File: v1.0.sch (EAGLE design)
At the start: 169 parts, among them J1 DC-044-A, J2 MICROSD-9P, J3 2p-2.54, J4 2p-2.54, Q1 SI4532ADY, Q3 6pF@32.7680kHz, SW1 SW-200D, SW2 SW-200D, U1 MCP23017-E/SO, U10 74HC139N, U11 BZX84C30, U2 MCP79412-I/SN, U3 LOPY, U4 GROVE_DC&DC, U5 LM1085IT-5.0, U6 FT232RL-SSOP28, U7 2x14p-2.54, U8 FT232RL-SSOP28, U9 SP483ECN-L, X1 JST-XH-05-PIN-ROUND-PAD, X10 JST-XH-07-PIN-ROUND-PAD, X11 JST-XH-07-PIN-ROUND-PAD, X12 JST-XH-07-PIN-ROUND-PAD, X13 JST-XH-05-PIN-ROUND-PAD, X14 JST-XH-05-PIN-ROUND-PAD, X15 JST-XH-05-PIN-ROUND-PAD, X16 JST-XH-05-PIN-ROUND-PAD, X17 JST-XH-05-PIN-ROUND-PAD, X18 JST-XH-05-PIN-ROUND-PAD, X19 JST-XH-05-PIN-ROUND-PAD, X2 JST-XH-05-PIN-ROUND-PAD, X20 JST-XH-05-PIN-ROUND-PAD, X21 JST-XH-05-PIN-ROUND-PAD, X22 JST-XH-07-PIN-ROUND-PAD, X23 JST-XH-05-PIN-ROUND-PAD, X24 JST-XH-07-PIN-ROUND-PAD, X25 JST-XH-07-PIN-ROUND-PAD, X27 JST-XH-07-PIN-ROUND-PAD, X28 JST-XH-05-PIN-ROUND-PAD, X3 JST-XH-05-PIN-ROUND-PAD, X4 JST-XH-07-PIN-ROUND-PAD, X5 JST-XH-07-PIN-ROUND-PAD, X6 JST-XH-07-PIN-ROUND-PAD, X7 JST-XH-07-PIN-ROUND-PAD, X8 JST-XH-07-PIN-ROUND-PAD, X9 JST-XH-07-PIN-ROUND-PAD

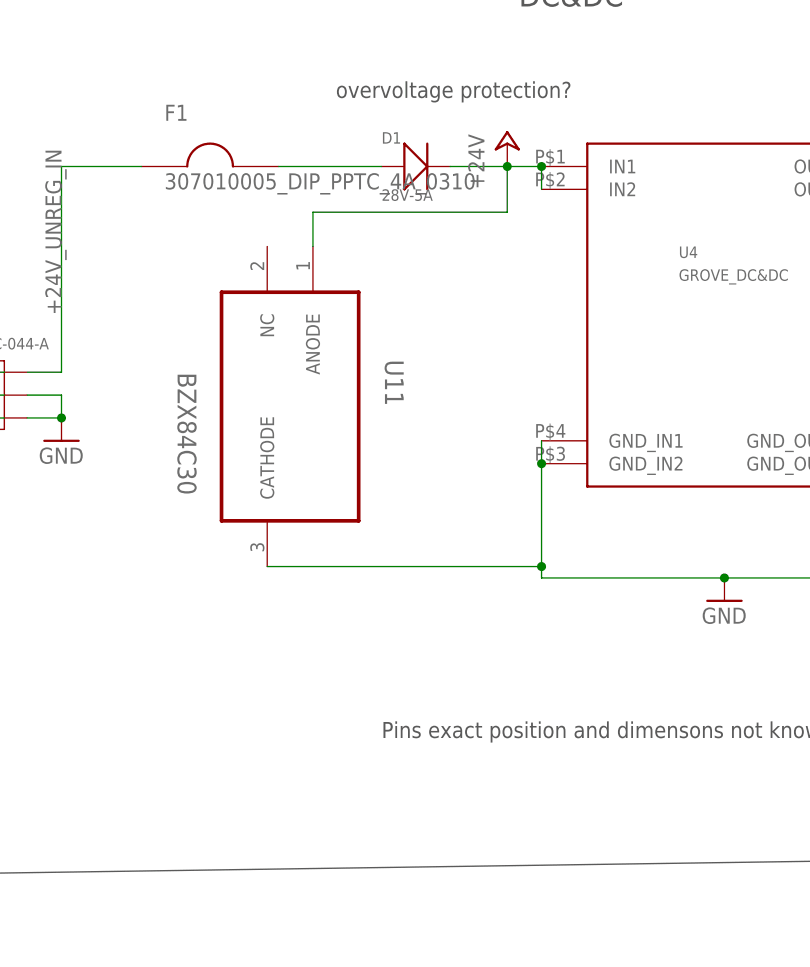
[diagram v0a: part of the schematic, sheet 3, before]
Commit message: overvoltage
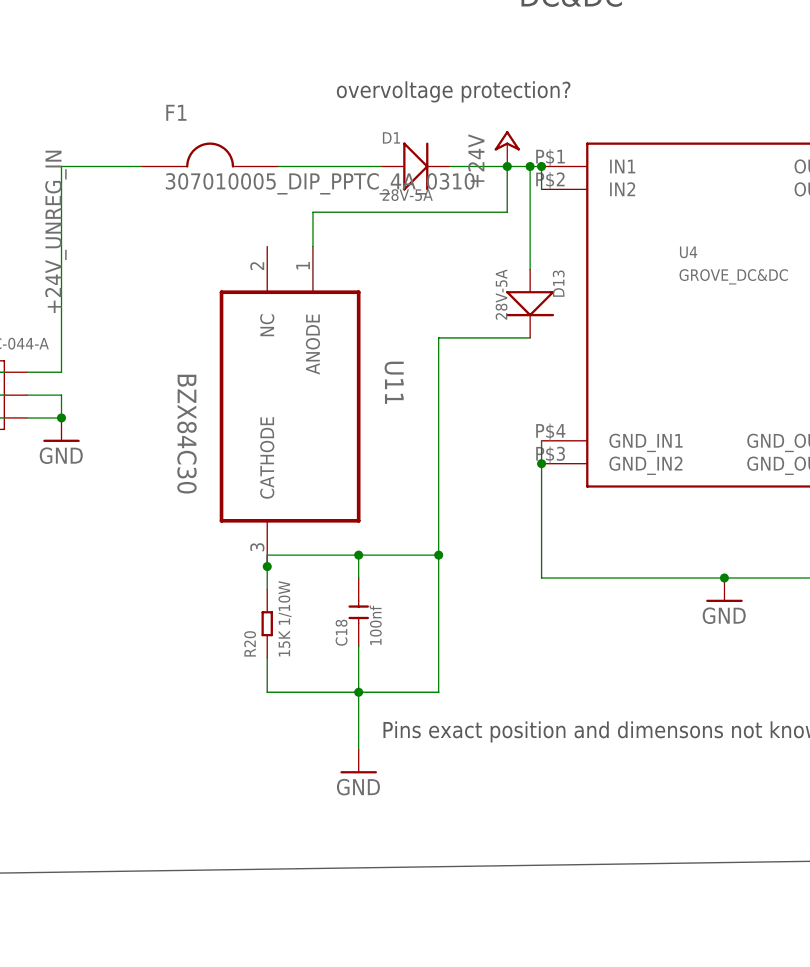
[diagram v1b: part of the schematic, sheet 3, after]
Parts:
- added C18: 100nf, Seeed-Capacitor:CERAMIC-100NF-50V-10%-X7R(0603)
- added D13: 28V-5A, Seeed-Diode-2016:SMD-DIODE-SCHOTTKY-28V-5A(DO-214AA)
- added R20: 15K 1/10W, Seeed-Resistor:SMD-RES-15K-1%-1/10W(0603)
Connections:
- net +24V: now also D13.+
- net GND: now also C18.1, C18.2, D13.-, R20.1, R20.2
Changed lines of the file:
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@@
 <part name="SW2" library="Seeed-Switch" library_urn="urn:adsk.eagle:library:476" deviceset="DIP-TILT-SWITCH-SW-200D(2P-12X3.6MM)" device="" value="SW-200D"/>
 <part name="GND41" library="supply1" library_urn="urn:adsk.eagle:library:371" deviceset="GND" device=""/>
+<part name="C18" library="Seeed-Capacitor" library_urn="urn:adsk.eagle:library:464" deviceset="CERAMIC-100NF-50V-10%-X7R(0603)" device="" value="100nf"/>
+<part name="R20" library="Seeed-Resistor" library_urn="urn:adsk.eagle:library:474" deviceset="SMD-RES-15K-1%-1/10W(0603)" device="" value="15K 1/10W"/>
+<part name="D13" library="Seeed-Diode-2016" library_urn="urn:adsk.eagle:library:453" deviceset="SMD-DIODE-SCHOTTKY-28V-5A(DO-214AA)" device="" value="28V-5A"/>
+<part name="GND40" library="supply1" library_urn="urn:adsk.eagle:library:371" deviceset="GND" device=""/>
 </parts>
 <sheets>
@@
 <instance part="SW2" gate="G$1" x="228.6" y="205.74" rot="R90"/>
 <instance part="GND41" gate="1" x="228.6" y="195.58"/>
+<instance part="C18" gate="G$1" x="60.96" y="181.61" rot="R90"/>
+<instance part="R20" gate="G$1" x="50.8" y="180.34" rot="R90"/>
+<instance part="D13" gate="G$1" x="80.01" y="215.9" rot="R270"/>
+<instance part="GND40" gate="1" x="60.96" y="163.83"/>
 </instances>
 <busses>
@@
 <pinref part="U4" gate="G$1" pin="GND_IN2"/>
 <wire x1="101.6" y1="185.42" x2="81.28" y2="185.42" width="0.1524" layer="91"/>
-<wire x1="81.28" y1="185.42" x2="81.28" y2="186.69" width="0.1524" layer="91"/>
 <pinref part="U4" gate="G$1" pin="GND_IN1"/>
-<wire x1="81.28" y1="186.69" x2="81.28" y2="198.12" width="0.1524" layer="91"/>
+<wire x1="81.28" y1="185.42" x2="81.28" y2="198.12" width="0.1524" layer="91"/>
 <wire x1="81.28" y1="198.12" x2="81.28" y2="200.66" width="0.1524" layer="91"/>
 <junction x="81.28" y="198.12"/>
@@
 <wire x1="121.92" y1="198.12" x2="121.92" y2="200.66" width="0.1524" layer="91"/>
 <junction x="121.92" y="198.12"/>
-<pinref part="U11" gate="A" pin="CATHODE"/>
-<wire x1="50.8" y1="186.69" x2="81.28" y2="186.69" width="0.1524" layer="91"/>
-<junction x="81.28" y="186.69"/>
 </segment>
 <segment>
@@
 <wire x1="228.6" y1="199.39" x2="228.6" y2="198.12" width="0.1524" layer="91"/>
 </segment>
+<segment>
+<pinref part="U11" gate="A" pin="CATHODE"/>
+<wire x1="50.8" y1="186.69" x2="50.8" y2="184.15" width="0.1524" layer="91"/>
+<pinref part="R20" gate="G$1" pin="2"/>
+<pinref part="D13" gate="G$1" pin="-"/>
+<wire x1="80.01" y1="212.09" x2="69.85" y2="212.09" width="0.1524" layer="91"/>
+<wire x1="69.85" y1="212.09" x2="69.85" y2="187.96" width="0.1524" layer="91"/>
+<wire x1="69.85" y1="187.96" x2="60.96" y2="187.96" width="0.1524" layer="91"/>
+<wire x1="60.96" y1="187.96" x2="50.8" y2="187.96" width="0.1524" layer="91"/>
+<wire x1="50.8" y1="187.96" x2="50.8" y2="186.69" width="0.1524" layer="91"/>
+<junction x="50.8" y="186.69"/>
+<wire x1="69.85" y1="187.96" x2="69.85" y2="172.72" width="0.1524" layer="91"/>
+<junction x="69.85" y="187.96"/>
+<pinref part="C18" gate="G$1" pin="2"/>
+<wire x1="60.96" y1="187.96" x2="60.96" y2="185.42" width="0.1524" layer="91"/>
+<junction x="60.96" y="187.96"/>
+<pinref part="R20" gate="G$1" pin="1"/>
+<wire x1="50.8" y1="176.53" x2="50.8" y2="172.72" width="0.1524" layer="91"/>
+<wire x1="50.8" y1="172.72" x2="60.96" y2="172.72" width="0.1524" layer="91"/>
+<pinref part="C18" gate="G$1" pin="1"/>
+<wire x1="60.96" y1="172.72" x2="69.85" y2="172.72" width="0.1524" layer="91"/>
+<wire x1="60.96" y1="177.8" x2="60.96" y2="172.72" width="0.1524" layer="91"/>
+<junction x="60.96" y="172.72"/>
+<wire x1="60.96" y1="172.72" x2="60.96" y2="166.37" width="0.1524" layer="91"/>
+<pinref part="GND40" gate="1" pin="GND"/>
+</segment>
 </net>
 <net name="+24V" class="0">
 <segment>
-<wire x1="77.47" y1="231.14" x2="81.28" y2="231.14" width="0.1524" layer="91"/>
+<wire x1="77.47" y1="231.14" x2="80.01" y2="231.14" width="0.1524" layer="91"/>
 <pinref part="D1" gate="G$1" pin="-"/>
+<wire x1="80.01" y1="231.14" x2="81.28" y2="231.14" width="0.1524" layer="91"/>
 <wire x1="71.12" y1="231.14" x2="77.47" y2="231.14" width="0.1524" layer="91"/>
 <junction x="77.47" y="231.14"/>
@@
 <wire x1="77.47" y1="226.06" x2="55.88" y2="226.06" width="0.1524" layer="91"/>
 <wire x1="55.88" y1="226.06" x2="55.88" y2="222.25" width="0.1524" layer="91"/>
-</segment>
-</net>
+<pinref part="D13" gate="G$1" pin="+"/>
+<wire x1="80.01" y1="231.14" x2="80.01" y2="219.71" width="0.1524" layer="91"/>
+<junction x="80.01" y="231.14"/>
+</segment>
+</net>

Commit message: Some tidying
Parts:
- removed D13: 28V-5A, Seeed-Diode-2016:SMD-DIODE-SCHOTTKY-28V-5A(DO-214AA)
- added F48, F49: SMD1206R500SF, Seeed-Fuse:SMD-PPTC-500MA(1206)
- added X26: JST-XH-05-PIN-ROUND-PAD, Rembrandt Electronics - JST XH Connectors v1-0 2:JST-XH-05-PIN-ROUND-PAD
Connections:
- removed net 3V3_SMOOTH1: F27.1, F27.2, X10-2.S
- removed net 3V3_SMOOTH2: F31.1, F31.2, X12-2.S
- removed net N$4 (its old number): USB1.ID
- new net N$56: F49.2, X26-2.S
- new net N$63: F76.2, U7.1, U7.28
- new net N$64: F77.2, U7.2, U7.27
- new net N$66: F75.2, X4-2.S
- new net N$67: F83.2, X3-2.S
- new net N$68: D1.+, F1.P$2
- new net N$69: F24.2, X10-1.S
- new net N$70: F27.2, X10-2.S
- new net N$71: F31.2, X12-2.S
- new net N$72: F33.2, X11-2.S
- new net N$73: F2.2, X8-2.S
- new net N$74: F29.2, X9-2.S
- net +24V: now also U11.CATHODE; no longer D13.+, U11.ANODE
- net +24V_UNREG_IN: no longer D1.+, F1.P$2
- net +5V: now also F48.1, F48.2, Q1P.S, X26-1.S; no longer C13.2, F28.1, F34.2, F46.2, F76.2, U7.1, U7.28, X23-1.S, X28-1.S
- net +5V1: no longer F24.2, X10-1.S
- net 3V3_SMOOTH: now also F10.1, F12.1, F14.1, F16.1, F18.1, F20.1, F22.1, F49.1, F6.1, F8.1; no longer F2.2, F29.2, F33.2, X11-2.S, X8-2.S, X9-2.S
- net GND: now also Q1N.S, R17.1, U11.ANODE, X26-3.S; no longer D13.-, SW2.2, U11.CATHODE
- net LOPY_3V3: now also SW2.1; no longer F10.1, F12.1, F14.1, F16.1, F18.1, F20.1, F22.1, F6.1, F75.2, F77.2, F8.1, F83.2, U7.2, U7.27, X3-2.S, X4-2.S
- net N$17: now also R16.1
- net N$25: now also F46.2, X28-1.S; no longer Q1P.S, R16.1
- net N$65: now also F34.2, X23-1.S; no longer Q1N.S, R17.1, SW2.1
- net PI_5V: now also C13.2
- net PI_PWR_CTRL: now also SW2.2
- net SCL_3V3: now also X26-5.S
- net SDA_3V3: now also X26-4.S
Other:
- moved on the sheet: F10, F11, F12, F13, F14, F15, F16, F17, F18, F19, F20, F21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

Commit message: tidy sockets
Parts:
- removed D10: RED-0603, Seeed-LED-2016:LED-SMD-RED-DIFFUSED(0603)
- removed R11: 1K, Seeed-Resistor-2016:SMD-RES-1K-1%-1/10W(0603)
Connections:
- removed net +5V4: F42.1, F42.2, X24-1.S
- removed net 3V3_SMOOTH4: F43.1, F43.2, X24-2.S
- removed net 3V3_SMOOTH5: F45.1, F45.2, X25-2.S
- new net +5V7: F44.2, X27-1.S
- new net 3V3_SMOOTH1: F39.2, X24-2.S
- new net 3V3_SMOOTH2: F43.2, X25-2.S
- new net 3V3_SMOOTH6: F45.2, X27-2.S
- new net N$75: F36.2, X9-1.S
- new net N$76: F37.2, X9-2.S
- net +5V: no longer F23.1, F26.1, F28.2, F3.1, F32.1, F34.1, F36.1, F36.2, F38.1, F38.2, F46.1, X27-1.S, X7-1.S, X9-1.S
- net +5V1: now also F38.2, X24-1.S; no longer F24.1
- net +5V2: no longer F30.1
- net +5V3: no longer F40.1
- net +5V5: now also F42.2; no longer F44.1, F44.2
- net 3V3_SMOOTH: now also F23.1, F26.1, F27.1, F3.1, F31.1, F41.1, F43.1, F45.1; no longer F2.1, F25.1, F37.2, F39.2, F4.1, X27-2.S, X7-2.S
- net 3V3_SMOOTH3: no longer F41.1
- net ADC1+: now also X22-4.S; no longer X27-4.S
- net ADC1-: now also X22-5.S; no longer X27-5.S
- net ADC2+: now also X22-6.S; no longer X27-6.S
- net ADC2-: now also X22-7.S; no longer X27-7.S
- net ADC3+: now also X24-4.S; no longer X22-4.S
- net ADC3-: now also X24-5.S; no longer X22-5.S
- net ADC4+: now also X24-6.S; no longer X22-6.S
- net ADC4-: now also X24-7.S; no longer X22-7.S
- net ADC5+: now also X25-4.S; no longer X24-4.S
- net ADC5-: now also X25-5.S; no longer X24-5.S
- net ADC6+: now also X25-6.S; no longer X24-6.S
- net ADC6-: now also X25-7.S; no longer X24-7.S
- net ADC7+: now also X27-4.S; no longer X25-4.S
- net ADC7-: now also X27-5.S; no longer X25-5.S
- net ADC8+: now also X27-6.S; no longer X25-6.S
- net ADC8-: now also X27-7.S; no longer X25-7.S
- net N$23: no longer D10.-
- net N$28: now also F2.2, X5-1.S; no longer D10.+, R11.1
- net N$46: now also F3.2; no longer F4.2
- net N$57: now also F4.2, X6-1.S; no longer F25.2, X6-2.S
- net N$58: now also X6-2.S; no longer X6-1.S
- net N$59: now also F25.2, X7-1.S; no longer F3.2, X5-1.S
- net N$60: now also X7-2.S; no longer X8-1.S
- net N$73: now also F28.2, X8-1.S; no longer F2.2, X8-2.S
- net N$74: now also X8-2.S; no longer X9-2.S
- net PI_5V: now also F2.1, F24.1, F25.1, F28.1, F30.1, F32.1, F34.1, F36.1, F38.1, F4.1, F40.1, F42.1, F44.1, F46.1
- net RPI_CS1: now also X8-7.S; no longer X5-7.S
- net RPI_CS2: now also X9-7.S; no longer X6-7.S
- net RPI_CS3: now also X6-7.S; no longer X7-7.S
- net RPI_CS4: now also X7-7.S; no longer X8-7.S
- net RPI_CS5: now also X5-7.S; no longer X9-7.S
- net SPI_MISO: now also X5-5.S, X6-5.S, X7-5.S, X9-5.S; no longer X5-4.S, X6-4.S, X7-4.S, X9-4.S
- net SPI_MOSI: now also X5-4.S, X6-4.S, X7-4.S, X9-4.S; no longer X5-5.S, X6-5.S, X7-5.S, X9-5.S
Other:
- note removed: "Done up to 3V3_SMOOTH"
- note removed: "Work out all required resitor values"
- moved on the sheet: F2, F23, F24, F25, F26, F27, F28, F29, F3, F30, F31, F32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

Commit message: mcp23017 socket
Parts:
- added J5, J6: 16p-2.54, Seeed-Connector:DIP-BLACK-MALE-HEADER-VERT(16P-2.54)
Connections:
- net N$12: now also J5.2, J6.2
- net N$13: now also J5.3, J6.3
- net N$14: now also J5.4, J6.4
- net N$15: now also J5.5, J6.5
- net N$16: now also J5.6, J6.6
- net N$19: now also J5.7, J6.7
- net N$22: now also J5.8, J6.8
- net N$24: now also J5.9, J6.9
- net N$26: now also J5.10, J6.10
- net N$27: now also J5.11, J6.11
- net N$35: now also J5.12, J6.12
- net N$36: now also J5.13, J6.13
- net N$37: now also J5.14, J6.14
- net N$39: now also J5.15, J6.15
- net N$40: now also J5.16, J6.16
- net N$8: now also J5.1, J6.1
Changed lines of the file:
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@@
 <part name="F44" library="Seeed-Fuse" library_urn="urn:adsk.eagle:library:469" deviceset="SMD-PPTC-500MA(1206)" device="" value="SMD1206R500SF"/>
 <part name="F45" library="Seeed-Fuse" library_urn="urn:adsk.eagle:library:469" deviceset="SMD-PPTC-500MA(1206)" device="" value="SMD1206R500SF"/>
+<part name="J5" library="Seeed-Connector" library_urn="urn:adsk.eagle:library:465" deviceset="DIP-BLACK-MALE-HEADER-VERT(16P-2.54)" device="" value="16p-2.54"/>
+<part name="J6" library="Seeed-Connector" library_urn="urn:adsk.eagle:library:465" deviceset="DIP-BLACK-MALE-HEADER-VERT(16P-2.54)" device="" value="16p-2.54"/>
 </parts>
 <sheets>
@@
 <instance part="R19" gate="G$1" x="331.47" y="228.6" rot="R90"/>
 <instance part="+3V9" gate="G$1" x="323.85" y="237.49"/>
+<instance part="J5" gate="G$1" x="264.16" y="200.66"/>
+<instance part="J6" gate="G$1" x="281.94" y="200.66"/>
 </instances>
 <busses>
@@
 <segment>
 <pinref part="U1" gate="A" pin="GPA0"/>
-<wire x1="238.76" y1="220.98" x2="250.19" y2="220.98" width="0.1524" layer="91"/>
+<wire x1="238.76" y1="220.98" x2="256.54" y2="220.98" width="0.1524" layer="91"/>
+<pinref part="J5" gate="G$1" pin="1"/>
+<pinref part="J6" gate="G$1" pin="1"/>
+<wire x1="256.54" y1="220.98" x2="274.32" y2="220.98" width="0.1524" layer="91"/>
+<junction x="256.54" y="220.98"/>
 </segment>
 </net>
@@
 <segment>
 <pinref part="U1" gate="A" pin="GPA1"/>
-<wire x1="238.76" y1="218.44" x2="250.19" y2="218.44" width="0.1524" layer="91"/>
+<wire x1="238.76" y1="218.44" x2="256.54" y2="218.44" width="0.1524" layer="91"/>
+<pinref part="J5" gate="G$1" pin="2"/>
+<pinref part="J6" gate="G$1" pin="2"/>
+<wire x1="256.54" y1="218.44" x2="274.32" y2="218.44" width="0.1524" layer="91"/>
+<junction x="256.54" y="218.44"/>
 </segment>
 </net>
@@
 <segment>
 <pinref part="U1" gate="A" pin="GPA2"/>
-<wire x1="238.76" y1="215.9" x2="250.19" y2="215.9" width="0.1524" layer="91"/>
+<wire x1="238.76" y1="215.9" x2="256.54" y2="215.9" width="0.1524" layer="91"/>
+<pinref part="J5" gate="G$1" pin="3"/>
+<pinref part="J6" gate="G$1" pin="3"/>
+<wire x1="256.54" y1="215.9" x2="274.32" y2="215.9" width="0.1524" layer="91"/>
+<junction x="256.54" y="215.9"/>
 </segment>
 </net>
@@
 <segment>
 <pinref part="U1" gate="A" pin="GPA3"/>
-<wire x1="238.76" y1="213.36" x2="250.19" y2="213.36" width="0.1524" layer="91"/>
+<wire x1="238.76" y1="213.36" x2="256.54" y2="213.36" width="0.1524" layer="91"/>
+<pinref part="J5" gate="G$1" pin="4"/>
+<pinref part="J6" gate="G$1" pin="4"/>
+<wire x1="256.54" y1="213.36" x2="274.32" y2="213.36" width="0.1524" layer="91"/>
+<junction x="256.54" y="213.36"/>
 </segment>
 </net>
@@
 <segment>
 <pinref part="U1" gate="A" pin="GPA4"/>
-<wire x1="238.76" y1="210.82" x2="250.19" y2="210.82" width="0.1524" layer="91"/>
+<wire x1="238.76" y1="210.82" x2="256.54" y2="210.82" width="0.1524" layer="91"/>
+<pinref part="J5" gate="G$1" pin="5"/>
+<pinref part="J6" gate="G$1" pin="5"/>
+<wire x1="256.54" y1="210.82" x2="274.32" y2="210.82" width="0.1524" layer="91"/>
+<junction x="256.54" y="210.82"/>
 </segment>
 </net>
@@
 <segment>
 <pinref part="U1" gate="A" pin="GPA5"/>
-<wire x1="238.76" y1="208.28" x2="250.19" y2="208.28" width="0.1524" layer="91"/>
+<wire x1="238.76" y1="208.28" x2="256.54" y2="208.28" width="0.1524" layer="91"/>
+<pinref part="J5" gate="G$1" pin="6"/>
+<pinref part="J6" gate="G$1" pin="6"/>
+<wire x1="256.54" y1="208.28" x2="274.32" y2="208.28" width="0.1524" layer="91"/>
+<junction x="256.54" y="208.28"/>
 </segment>
 </net>
@@
 <segment>
 <pinref part="U1" gate="A" pin="GPA6"/>
-<wire x1="238.76" y1="205.74" x2="250.19" y2="205.74" width="0.1524" layer="91"/>
+<wire x1="238.76" y1="205.74" x2="256.54" y2="205.74" width="0.1524" layer="91"/>
+<pinref part="J5" gate="G$1" pin="7"/>
+<pinref part="J6" gate="G$1" pin="7"/>
+<wire x1="256.54" y1="205.74" x2="274.32" y2="205.74" width="0.1524" layer="91"/>
+<junction x="256.54" y="205.74"/>
 </segment>
 </net>
@@
 <segment>
 <pinref part="U1" gate="A" pin="GPA7"/>
-<wire x1="238.76" y1="203.2" x2="250.19" y2="203.2" width="0.1524" layer="91"/>
+<wire x1="238.76" y1="203.2" x2="256.54" y2="203.2" width="0.1524" layer="91"/>
+<pinref part="J5" gate="G$1" pin="8"/>
+<pinref part="J6" gate="G$1" pin="8"/>
+<wire x1="256.54" y1="203.2" x2="274.32" y2="203.2" width="0.1524" layer="91"/>
+<junction x="256.54" y="203.2"/>
 </segment>
 </net>
@@
 <segment>
 <pinref part="U1" gate="A" pin="GPB0"/>
-<wire x1="238.76" y1="200.66" x2="250.19" y2="200.66" width="0.1524" layer="91"/>
+<wire x1="238.76" y1="200.66" x2="256.54" y2="200.66" width="0.1524" layer="91"/>
+<pinref part="J5" gate="G$1" pin="9"/>
+<pinref part="J6" gate="G$1" pin="9"/>
+<wire x1="256.54" y1="200.66" x2="274.32" y2="200.66" width="0.1524" layer="91"/>
+<junction x="256.54" y="200.66"/>
 </segment>
 </net>
@@
 <segment>
 <pinref part="U1" gate="A" pin="GPB1"/>
-<wire x1="238.76" y1="198.12" x2="250.19" y2="198.12" width="0.1524" layer="91"/>
+<wire x1="238.76" y1="198.12" x2="256.54" y2="198.12" width="0.1524" layer="91"/>
+<pinref part="J5" gate="G$1" pin="10"/>
+<pinref part="J6" gate="G$1" pin="10"/>
+<wire x1="274.32" y1="198.12" x2="256.54" y2="198.12" width="0.1524" layer="91"/>
+<junction x="256.54" y="198.12"/>
 </segment>
 </net>
@@
 <segment>
 <pinref part="U1" gate="A" pin="GPB2"/>
-<wire x1="238.76" y1="195.58" x2="250.19" y2="195.58" width="0.1524" layer="91"/>
+<wire x1="238.76" y1="195.58" x2="256.54" y2="195.58" width="0.1524" layer="91"/>
+<pinref part="J5" gate="G$1" pin="11"/>
+<pinref part="J6" gate="G$1" pin="11"/>
+<wire x1="256.54" y1="195.58" x2="274.32" y2="195.58" width="0.1524" layer="91"/>
+<junction x="256.54" y="195.58"/>
 </segment>
 </net>
@@
 <segment>
 <pinref part="U1" gate="A" pin="GPB3"/>
-<wire x1="238.76" y1="193.04" x2="250.19" y2="193.04" width="0.1524" layer="91"/>
+<wire x1="238.76" y1="193.04" x2="256.54" y2="193.04" width="0.1524" layer="91"/>
+<pinref part="J5" gate="G$1" pin="12"/>
+<pinref part="J6" gate="G$1" pin="12"/>
+<wire x1="256.54" y1="193.04" x2="274.32" y2="193.04" width="0.1524" layer="91"/>
+<junction x="256.54" y="193.04"/>
 </segment>
 </net>
@@
 <segment>
 <pinref part="U1" gate="A" pin="GPB4"/>
-<wire x1="238.76" y1="190.5" x2="250.19" y2="190.5" width="0.1524" layer="91"/>
+<wire x1="238.76" y1="190.5" x2="256.54" y2="190.5" width="0.1524" layer="91"/>
+<pinref part="J5" gate="G$1" pin="13"/>
+<pinref part="J6" gate="G$1" pin="13"/>
+<wire x1="256.54" y1="190.5" x2="274.32" y2="190.5" width="0.1524" layer="91"/>
+<junction x="256.54" y="190.5"/>
 </segment>
 </net>
@@
 <segment>
 <pinref part="U1" gate="A" pin="GPB5"/>
-<wire x1="238.76" y1="187.96" x2="250.19" y2="187.96" width="0.1524" layer="91"/>
+<wire x1="238.76" y1="187.96" x2="256.54" y2="187.96" width="0.1524" layer="91"/>
+<pinref part="J5" gate="G$1" pin="14"/>
+<pinref part="J6" gate="G$1" pin="14"/>
+<wire x1="256.54" y1="187.96" x2="274.32" y2="187.96" width="0.1524" layer="91"/>
+<junction x="256.54" y="187.96"/>
 </segment>
 </net>
@@
 <segment>
 <pinref part="U1" gate="A" pin="GPB6"/>
-<wire x1="238.76" y1="185.42" x2="250.19" y2="185.42" width="0.1524" layer="91"/>
+<wire x1="238.76" y1="185.42" x2="256.54" y2="185.42" width="0.1524" layer="91"/>
+<pinref part="J5" gate="G$1" pin="15"/>
+<pinref part="J6" gate="G$1" pin="15"/>
+<wire x1="256.54" y1="185.42" x2="274.32" y2="185.42" width="0.1524" layer="91"/>
+<junction x="256.54" y="185.42"/>
 </segment>
 </net>
@@
 <segment>
 <pinref part="U1" gate="A" pin="GPB7"/>
-<wire x1="238.76" y1="182.88" x2="250.19" y2="182.88" width="0.1524" layer="91"/>
-</segment>
-</net>
+<wire x1="238.76" y1="182.88" x2="256.54" y2="182.88" width="0.1524" layer="91"/>
+<pinref part="J5" gate="G$1" pin="16"/>
+<pinref part="J6" gate="G$1" pin="16"/>
+<wire x1="256.54" y1="182.88" x2="274.32" y2="182.88" width="0.1524" layer="91"/>
+<junction x="256.54" y="182.88"/>
+</segment>
+</net>
